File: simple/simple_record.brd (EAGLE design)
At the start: 8 parts, among them J1 SQUALL_HEADER, Q1 MOSFET-NCHANNELSMD, U2 MAX9939

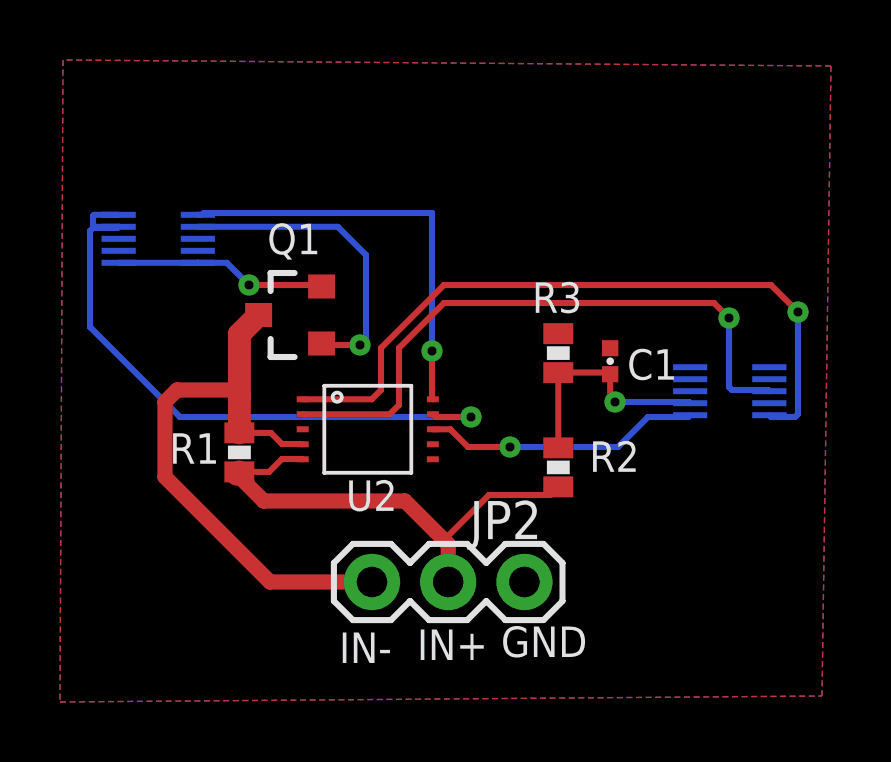
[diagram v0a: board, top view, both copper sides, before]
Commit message: added the files being sent to fab
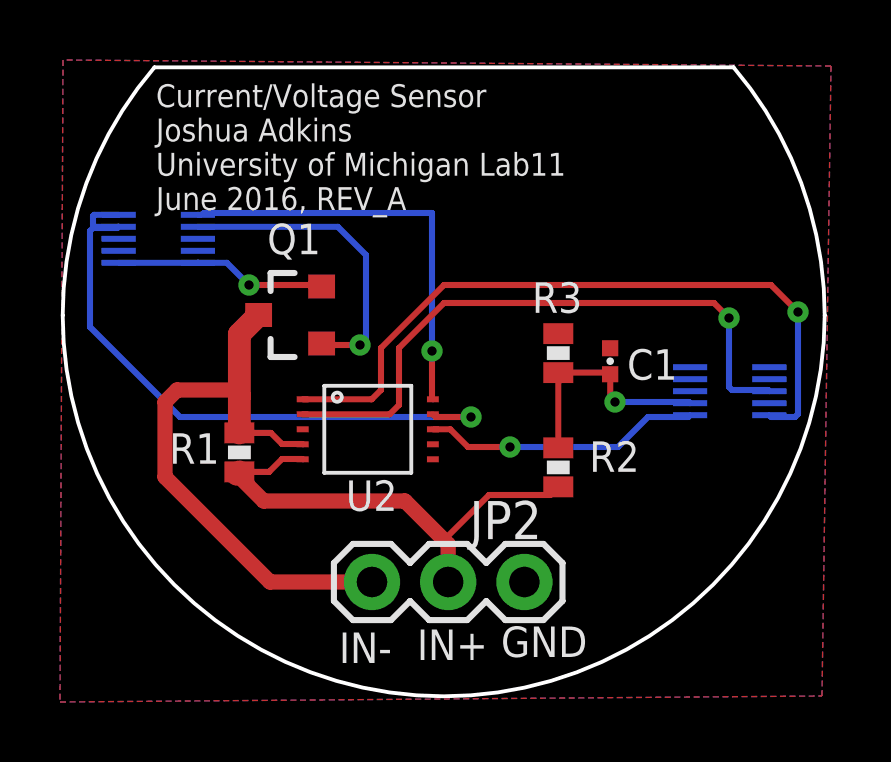
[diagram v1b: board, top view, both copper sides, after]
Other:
- board outline added: 25.4 x 21 mm
- board text added: "Current/Voltage Sensor Joshua Adkins University of Michigan Lab11 June 2016, REV_A"
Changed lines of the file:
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@@
 <setting verticaltext="up"/>
 </settings>
-<grid distance="0.1" unitdist="mm" unit="mm" style="lines" multiple="1" display="no" altdistance="0.025" altunitdist="inch" altunit="inch"/>
+<grid distance="0.01" unitdist="mm" unit="mm" style="lines" multiple="1" display="no" altdistance="0.025" altunitdist="inch" altunit="inch"/>
 <layers>
 <layer number="1" name="Top" color="4" fill="1" visible="yes" active="yes"/>
@@
 <board>
 <plain>
-<text x="9.2" y="1.1" size="1.016" layer="21">IN-</text>
-<text x="11.8" y="1.2" size="1.016" layer="21">IN+</text>
-<text x="14.6" y="1.3" size="1.016" layer="21">GND</text>
+<text x="9.2" y="1.1" size="1.016" layer="21" font="vector">IN-</text>
+<text x="11.8" y="1.2" size="1.016" layer="21" font="vector">IN+</text>
+<text x="14.6" y="1.3" size="1.016" layer="21" font="vector">GND</text>
+<text x="3.1" y="16.2" size="0.762" layer="25" font="vector">Current/Voltage Sensor
+Joshua Adkins
+University of Michigan Lab11
+June 2016, REV_A</text>
+<wire x1="4.665" y1="17.5" x2="4.665" y2="16.2" width="0.127" layer="22"/>
+<wire x1="4.665" y1="14.2" x2="4.665" y2="12.9" width="0.127" layer="22"/>
+<wire x1="4.665" y1="12.9" x2="1.785" y2="12.9" width="0.127" layer="22"/>
+<wire x1="1.785" y1="12.9" x2="1.785" y2="14.2" width="0.127" layer="22"/>
+<wire x1="1.785" y1="16.2" x2="1.785" y2="17.5" width="0.127" layer="22"/>
+<wire x1="1.785" y1="17.5" x2="4.665" y2="17.5" width="0.127" layer="22"/>
+<wire x1="4.025" y1="17" x2="4.025" y2="13.4" width="0.127" layer="52"/>
+<wire x1="4.025" y1="13.4" x2="2.425" y2="13.4" width="0.127" layer="52"/>
+<wire x1="2.425" y1="13.4" x2="2.425" y2="17" width="0.127" layer="52"/>
+<wire x1="2.425" y1="17" x2="4.025" y2="17" width="0.127" layer="52"/>
+<wire x1="23.715" y1="12.42" x2="23.715" y2="11.12" width="0.127" layer="22"/>
+<wire x1="23.715" y1="9.12" x2="23.715" y2="7.82" width="0.127" layer="22"/>
+<wire x1="23.715" y1="7.82" x2="20.835" y2="7.82" width="0.127" layer="22"/>
+<wire x1="20.835" y1="7.82" x2="20.835" y2="9.12" width="0.127" layer="22"/>
+<wire x1="20.835" y1="11.12" x2="20.835" y2="12.42" width="0.127" layer="22"/>
+<wire x1="20.835" y1="12.42" x2="23.715" y2="12.42" width="0.127" layer="22"/>
+<wire x1="23.075" y1="11.92" x2="23.075" y2="8.32" width="0.127" layer="52"/>
+<wire x1="23.075" y1="8.32" x2="21.475" y2="8.32" width="0.127" layer="52"/>
+<wire x1="21.475" y1="8.32" x2="21.475" y2="11.92" width="0.127" layer="52"/>
+<wire x1="21.475" y1="11.92" x2="23.075" y2="11.92" width="0.127" layer="52"/>
+<wire x1="25.39" y1="12.69" x2="-0.01" y2="12.69" width="0.127" layer="20" curve="-180"/>
+<wire x1="3.048" y1="20.955" x2="22.352" y2="20.955" width="0.127" layer="20"/>
+<wire x1="-0.01" y1="12.69" x2="3.048" y2="20.955" width="0.127" layer="20" curve="-40.54"/>
+<wire x1="25.39" y1="12.69" x2="22.352" y2="20.955" width="0.127" layer="20" curve="40.54"/>
 </plain>
 <attributes>
@@
 <element name="U2" library="chips" package="UMAX10" value="MAX9939" x="10.16" y="8.89" smashed="yes" rot="R270">
 <attribute name="DIGIKEY" value="MAX9939AUB+-ND" x="-12.7" y="-24.13" size="1.778" layer="27" rot="R270" display="off"/>
-<attribute name="NAME" x="9.43" y="6.17" size="1.016" layer="21"/>
+<attribute name="NAME" x="9.43" y="6.17" size="1.016" layer="21" font="vector"/>
 </element>
 <element name="Q1" library="fets" package="SOT23-3" value="MOSFET-NCHANNELSMD" x="7.62" y="12.7" smashed="yes" rot="R90">
@@
 </element>
 <element name="JP2" library="SparkFun-Connectors" package="1X03" value="" x="10.3" y="3.8" smashed="yes">
-<attribute name="NAME" x="13.5538" y="5.2288" size="1.27" layer="25" ratio="10"/>
+<attribute name="NAME" x="13.5538" y="5.2288" size="1.27" layer="25" font="vector" ratio="10"/>
 <attribute name="VALUE" x="9.03" y="0.625" size="1.27" layer="27"/>
 </element>
@@
 </board>
 </drawing>
+<compatibility>
+<note version="6.3" minversion="6.2.2" severity="warning">
+Since Version 6.2.2 text objects can contain more than one line,
+which will not be processed correctly with this version.
+</note>
+</compatibility>
 </eagle>
